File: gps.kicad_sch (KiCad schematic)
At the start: 9 parts, among them J6 SMA, U1 MAX-M10S

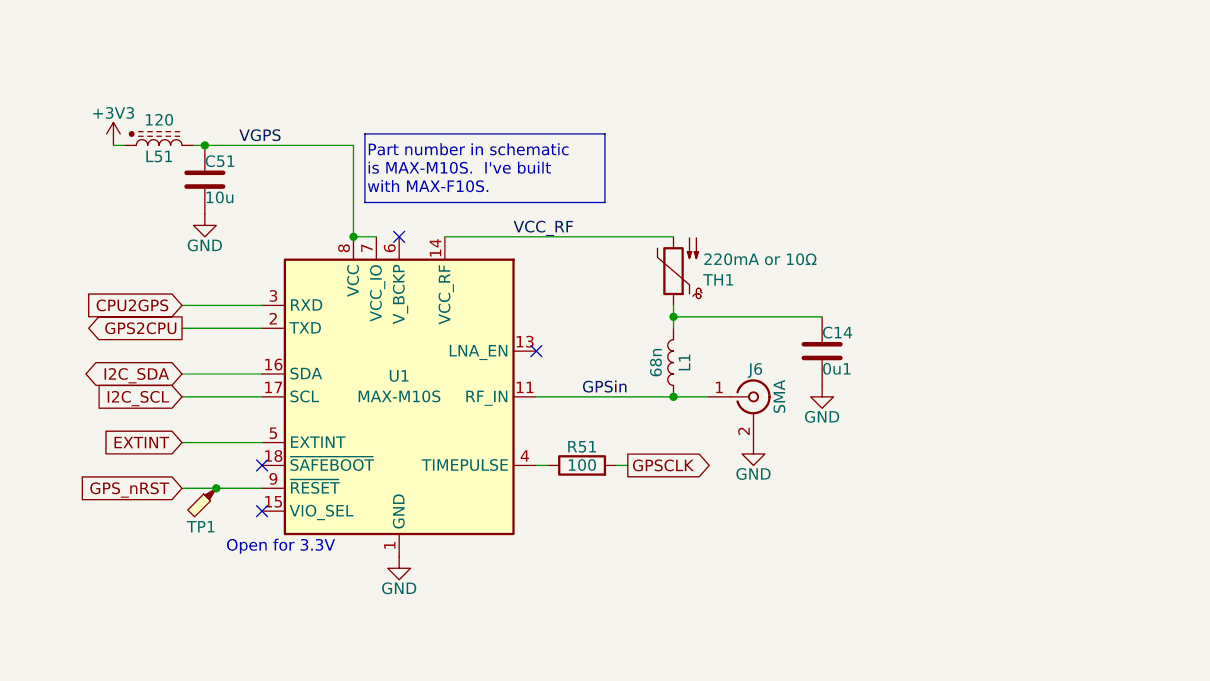
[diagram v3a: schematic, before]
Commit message: Pull-up on safe-boot.  Juggle things a bit.
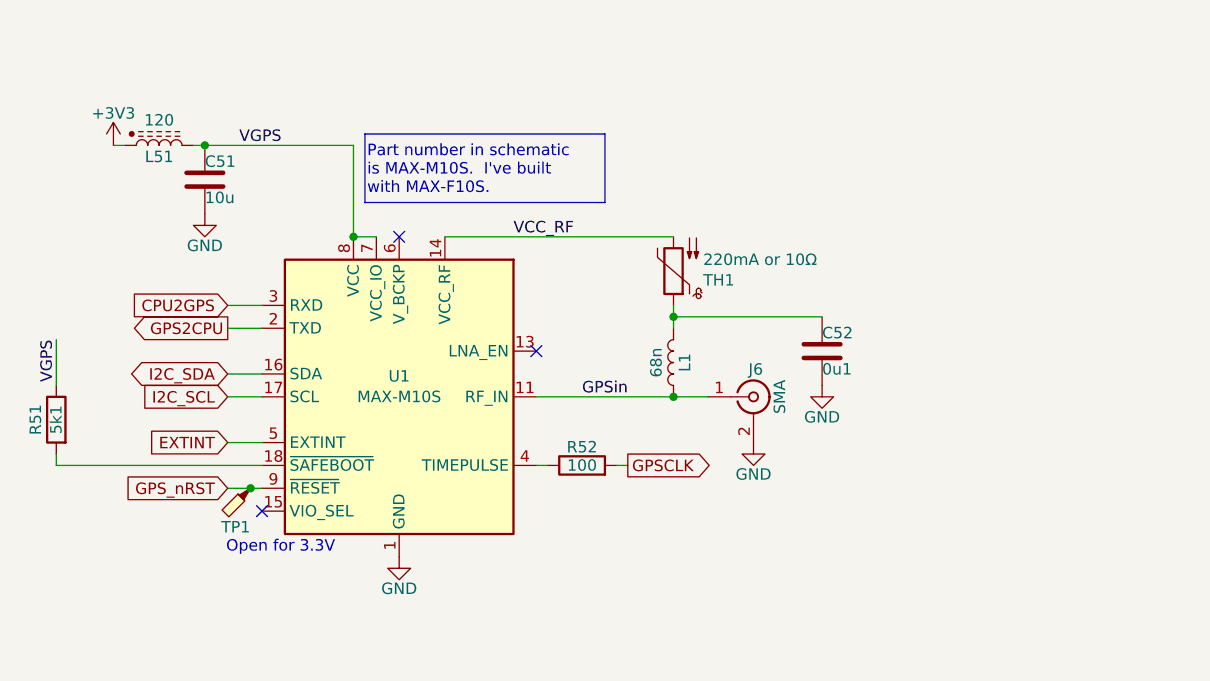
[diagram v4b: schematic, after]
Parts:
- added R51: 5k1, Resistor_SMD:R_0402_1005Metric, symbol Device:R
- renumbered C14 to C52, R51 to R52
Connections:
- net VGPS: now also R51.1
- net at U1.18 (~{SAFEBOOT}): now also R51.2
- no-connect marks 4 -> 3
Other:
- moved on the sheet: TP1
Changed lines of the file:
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@@
-	)
-	(junction
-		(at 80.01 109.22)
-		(diameter 0)
-		(color 0 0 0 0)
 	)
 	(junction
@@
 	)
 	(junction
+		(at 83.82 109.22)
+		(diameter 0)
+		(color 0 0 0 0)
+	)
+	(junction
 		(at 95.25 81.28)
 		(diameter 0)
@@
 	)
 	(no_connect
-		(at 85.09 106.68)
-	)
-	(no_connect
 		(at 100.33 81.28)
 	)
@@
 	(wire
 		(pts
-			(xy 80.01 109.22) (xy 85.09 109.22)
-		)
-		(stroke
-			(width 0)
-			(type default)
-		)
-	)
-	(wire
-		(pts
-			(xy 76.2 96.52) (xy 85.09 96.52)
+			(xy 81.28 96.52) (xy 85.09 96.52)
 		)
 		(stroke
@@
 	(wire
 		(pts
-			(xy 76.2 91.44) (xy 85.09 91.44)
+			(xy 81.28 91.44) (xy 85.09 91.44)
 		)
 		(stroke
@@
 	(wire
 		(pts
-			(xy 76.2 109.22) (xy 80.01 109.22)
+			(xy 81.28 109.22) (xy 83.82 109.22)
 		)
 		(stroke
@@
 	(wire
 		(pts
-			(xy 76.2 104.14) (xy 85.09 104.14)
+			(xy 62.23 106.68) (xy 85.09 106.68)
+		)
+		(stroke
+			(width 0)
+			(type default)
+		)
+	)
+	(wire
+		(pts
+			(xy 62.23 92.71) (xy 62.23 97.79)
+		)
+		(stroke
+			(width 0)
+			(type default)
+		)
+	)
+	(wire
+		(pts
+			(xy 81.28 104.14) (xy 85.09 104.14)
 		)
 		(stroke
@@
 	(wire
 		(pts
+			(xy 62.23 105.41) (xy 62.23 106.68)
+		)
+		(stroke
+			(width 0)
+			(type default)
+		)
+	)
+	(wire
+		(pts
 			(xy 130.81 88.9) (xy 130.81 90.17)
 		)
@@
 	(wire
 		(pts
-			(xy 76.2 88.9) (xy 85.09 88.9)
+			(xy 81.28 88.9) (xy 85.09 88.9)
 		)
 		(stroke
@@
 	(wire
 		(pts
-			(xy 76.2 99.06) (xy 85.09 99.06)
+			(xy 83.82 109.22) (xy 85.09 109.22)
+		)
+		(stroke
+			(width 0)
+			(type default)
+		)
+	)
+	(wire
+		(pts
+			(xy 81.28 99.06) (xy 85.09 99.06)
 		)
 		(stroke
@@
 	)
 	(label "VGPS"
+		(at 62.23 92.71 270)
+		(effects
+			(font
+				(size 1.27 1.27)
+			)
+			(justify right bottom)
+		)
+	)
+	(label "VGPS"
 		(at 82.55 71.12 0)
 		(effects
@@
 	(global_label "I2C_SCL"
 		(shape input)
-		(at 76.2 99.06 180)
-		(fields_autoplaced yes)
+		(at 81.28 99.06 180)
 		(effects
 			(font
@@
 		)
 		(property "Intersheetrefs" "${INTERSHEET_REFS}"
-			(at 65.6553 99.06 0)
+			(at 72.2593 99.06 0)
 			(show_name no)
 			(do_not_autoplace no)
@@
 	(global_label "I2C_SDA"
 		(shape bidirectional)
-		(at 76.2 96.52 180)
-		(fields_autoplaced yes)
+		(at 81.28 96.52 180)
 		(effects
 			(font
@@
 		)
 		(property "Intersheetrefs" "${INTERSHEET_REFS}"
-			(at 64.4835 96.52 0)
+			(at 71.0875 96.52 0)
 			(show_name no)
 			(do_not_autoplace no)
@@
 	(global_label "GPS2CPU"
 		(shape output)
-		(at 76.2 91.44 180)
-		(fields_autoplaced yes)
+		(at 81.28 91.44 180)
 		(effects
 			(font
@@
 		)
 		(property "Intersheetrefs" "${INTERSHEET_REFS}"
-			(at 64.3853 91.44 0)
+			(at 69.9733 91.44 0)
 			(show_name no)
 			(do_not_autoplace no)
@@
 	(global_label "GPS_nRST"
 		(shape input)
-		(at 76.2 109.22 180)
+		(at 81.28 109.22 180)
 		(fields_autoplaced yes)
 		(effects
@@
 		)
 		(property "Intersheetrefs" "${INTERSHEET_REFS}"
-			(at 63.9016 109.22 0)
+			(at 68.9816 109.22 0)
 			(show_name no)
 			(do_not_autoplace no)
@@
 	(global_label "CPU2GPS"
 		(shape input)
-		(at 76.2 88.9 180)
-		(fields_autoplaced yes)
+		(at 81.28 88.9 180)
 		(effects
 			(font
@@
 		)
 		(property "Intersheetrefs" "${INTERSHEET_REFS}"
-			(at 64.3853 88.9 0)
+			(at 70.7353 88.9 0)
 			(show_name no)
 			(do_not_autoplace no)
@@
 	(global_label "EXTINT"
 		(shape input)
-		(at 76.2 104.14 180)
+		(at 81.28 104.14 180)
 		(effects
 			(font
@@
 		)
 		(property "Intersheetrefs" "${INTERSHEET_REFS}"
-			(at 67.6509 104.14 0)
+			(at 73.4929 104.14 0)
 			(show_name no)
 			(do_not_autoplace no)
@@
 	(symbol
 		(lib_id "Connector:TestPoint_Probe")
-		(at 80.01 109.22 180)
+		(at 83.82 109.22 180)
 		(unit 1)
 		(body_style 1)
@@
 		(dnp no)
 		(property "Reference" "TP1"
-			(at 78.359 113.538 0)
+			(at 82.169 113.538 0)
 			(show_name no)
 			(do_not_autoplace no)
@@
 		)
 		(property "Value" "TestPoint_Probe"
-			(at 78.359 113.284 0)
+			(at 82.169 113.284 0)
 			(hide yes)
 			(show_name no)
@@
 		)
 		(property "Footprint" "Parts:TestPoint"
-			(at 74.93 109.22 0)
+			(at 78.74 109.22 0)
 			(hide yes)
 			(show_name no)
@@
 		)
 		(property "Datasheet" ""
-			(at 74.93 109.22 0)
+			(at 78.74 109.22 0)
 			(hide yes)
 			(show_name no)
@@
 		)
 		(property "Description" "test point (alternative probe-style design)"
-			(at 80.01 109.22 0)
+			(at 83.82 109.22 0)
 			(hide yes)
 			(show_name no)
@@
 		)
 		(property "Stock" "N/A"
-			(at 80.01 109.22 0)
+			(at 83.82 109.22 0)
 			(hide yes)
 			(show_name no)
@@
 	)
 	(symbol
+		(lib_id "Device:R")
+		(at 62.23 101.6 0)
+		(mirror y)
+		(unit 1)
+		(body_style 1)
+		(exclude_from_sim no)
+		(in_bom yes)
+		(on_board yes)
+		(in_pos_files yes)
+		(dnp no)
+		(property "Reference" "R51"
+			(at 59.944 101.6 90)
+			(show_name no)
+			(do_not_autoplace no)
+			(effects
+				(font
+					(size 1.27 1.27)
+				)
+			)
+		)
+		(property "Value" "5k1"
+			(at 62.23 101.6 90)
+			(show_name no)
+			(do_not_autoplace no)
+			(effects
+				(font
+					(size 1.27 1.27)
+				)
+			)
+		)
+		(property "Footprint" "Resistor_SMD:R_0402_1005Metric"
+			(at 64.008 101.6 90)
+			(hide yes)
+			(show_name no)
+			(do_not_autoplace no)
+			(effects
+				(font
+					(size 1.27 1.27)
+				)
+			)
+		)
+		(property "Datasheet" ""
+			(at 62.23 101.6 0)
+			(hide yes)
+			(show_name no)
+			(do_not_autoplace no)
+			(effects
+				(font
+					(size 1.27 1.27)
+				)
+			)
+		)
+		(property "Description" "Resistor"
+			(at 62.23 101.6 0)
+			(hide yes)
+			(show_name no)
+			(do_not_autoplace no)
+			(effects
+				(font
+					(size 1.27 1.27)
+				)
+			)
+		)
+		(property "LCSC" "C25905"
+			(at 62.23 101.6 90)
+			(hide yes)
+			(show_name no)
+			(do_not_autoplace no)
+			(effects
+				(font
+					(size 1.27 1.27)
+				)
+			)
+		)
+		(property "Stock" "Basic"
+			(at 62.23 101.6 90)
+			(hide yes)
+			(show_name no)
+			(do_not_autoplace no)
+			(effects
+				(font
+					(size 1.27 1.27)
+				)
+			)
+		)
+		(pin "2"
+		)
+		(pin "1"
+		)
+		(instances
+			(project "gpsfreak"
+				(path "/3160ff17-81c2-4674-af97-e8d9acaf6b65/69331f4b-e5ad-4452-8850-5c5a77857efb"
+					(reference "R51")
+					(unit 1)
+				)
+			)
+		)
+	)
+	(symbol
 		(lib_id "Device:C")
 		(at 147.32 93.98 0)
@@
 		(in_pos_files yes)
 		(dnp no)
-		(property "Reference" "C14"
+		(property "Reference" "C52"
 			(at 147.32 92.71 0)
 			(show_name no)
@@
 			(project "gpsfreak"
 				(path "/3160ff17-81c2-4674-af97-e8d9acaf6b65/69331f4b-e5ad-4452-8850-5c5a77857efb"
-					(reference "C14")
+					(reference "C52")
 					(unit 1)
 				)
@@
 		(in_pos_files yes)
 		(dnp no)
-		(property "Reference" "R51"
+		(property "Reference" "R52"
 			(at 120.65 104.648 90)
 			(show_name no)
@@
 			(project "gpsfreak"
 				(path "/3160ff17-81c2-4674-af97-e8d9acaf6b65/69331f4b-e5ad-4452-8850-5c5a77857efb"
-					(reference "R51")
+					(reference "R52")
 					(unit 1)
 				)

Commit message: Ordered.
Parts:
- TH1: Stock Ok -> 3
- U1: Stock ORDER, 1 -> ORDER
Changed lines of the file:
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@@
 			)
 		)
-		(property "Stock" "Ok"
+		(property "Stock" "3"
 			(at 130.81 85.09 0)
 			(hide yes)
@@
 			)
 		)
-		(property "Stock" "ORDER, 1"
-			(at 100.33 99.06 0)
-			(hide yes)
+		(property "Stock" "ORDER"
+			(at 100.33 99.06 0)
+			(hide yes)

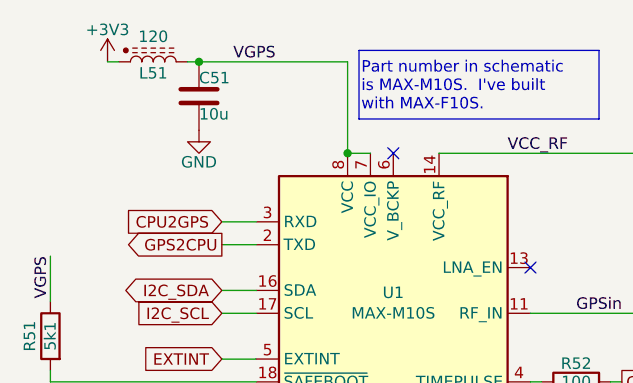
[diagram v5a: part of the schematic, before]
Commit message: Adjustments.  Silk screen clearance.
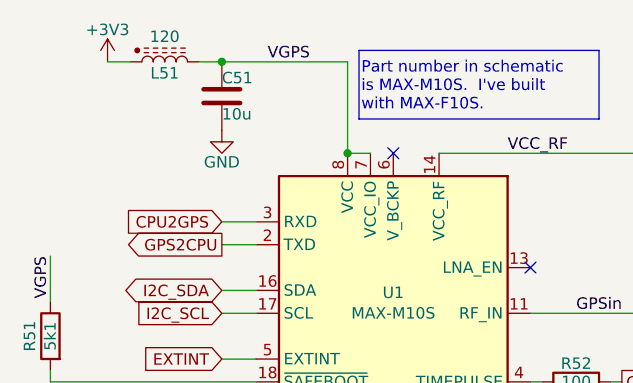
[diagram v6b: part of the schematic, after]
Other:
- moved on the sheet: C51, L51
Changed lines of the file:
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@@
-	)
-	(junction
-		(at 78.74 71.12)
-		(diameter 0)
-		(color 0 0 0 0)
 	)
 	(junction
@@
 	)
 	(junction
+		(at 81.28 71.12)
+		(diameter 0)
+		(color 0 0 0 0)
+	)
+	(junction
 		(at 83.82 109.22)
 		(diameter 0)
@@
 	(wire
 		(pts
+			(xy 81.28 71.12) (xy 95.25 71.12)
+		)
+		(stroke
+			(width 0)
+			(type default)
+		)
+	)
+	(wire
+		(pts
 			(xy 81.28 91.44) (xy 85.09 91.44)
 		)
@@
 	(wire
 		(pts
-			(xy 68.58 71.12) (xy 69.85 71.12)
+			(xy 68.58 71.12) (xy 71.12 71.12)
 		)
 		(stroke
@@
 	(wire
 		(pts
-			(xy 77.47 71.12) (xy 78.74 71.12)
-		)
-		(stroke
-			(width 0)
-			(type default)
-		)
-	)
-	(wire
-		(pts
-			(xy 78.74 71.12) (xy 95.25 71.12)
+			(xy 78.74 71.12) (xy 81.28 71.12)
 		)
 		(stroke
@@
 	)
 	(label "VGPS"
-		(at 82.55 71.12 0)
+		(at 86.36 71.12 0)
 		(effects
 			(font
@@
 		(shape input)
 		(at 81.28 109.22 180)
-		(fields_autoplaced yes)
 		(effects
 			(font
@@
 		)
 		(property "Intersheetrefs" "${INTERSHEET_REFS}"
-			(at 68.9816 109.22 0)
+			(at 70.2516 109.22 0)
 			(show_name no)
 			(do_not_autoplace no)
@@
 	(symbol
 		(lib_id "Parts:L_Ferrite_Power")
-		(at 73.66 71.12 90)
+		(at 74.93 71.12 90)
 		(unit 1)
 		(body_style 1)
@@
 		(dnp no)
 		(property "Reference" "L51"
-			(at 73.66 72.39 90)
+			(at 74.93 72.39 90)
 			(show_name no)
 			(do_not_autoplace no)
@@
 		)
 		(property "Value" "120"
-			(at 73.66 68.326 90)
+			(at 74.93 68.326 90)
 			(show_name no)
 			(do_not_autoplace no)
@@
 		)
 		(property "Footprint" "Inductor_SMD:L_0603_1608Metric"
-			(at 73.66 71.12 0)
+			(at 74.93 71.12 0)
 			(hide yes)
 			(show_name no)
@@
 		)
 		(property "Datasheet" ""
-			(at 73.66 71.12 0)
+			(at 74.93 71.12 0)
 			(hide yes)
 			(show_name no)
@@
 		)
 		(property "Description" "Inductor with ferrite core"
-			(at 73.66 71.12 0)
+			(at 74.93 71.12 0)
 			(hide yes)
 			(show_name no)
@@
 		)
 		(property "LCSC" "C14709"
-			(at 73.66 71.12 90)
+			(at 74.93 71.12 90)
 			(hide yes)
 			(show_name no)
@@
 		)
 		(property "Stock" "Basic"
-			(at 73.66 71.12 90)
+			(at 74.93 71.12 90)
 			(hide yes)
 			(show_name no)
@@
 	(symbol
 		(lib_id "Device:C")
-		(at 78.74 74.93 0)
+		(at 81.28 74.93 0)
 		(unit 1)
 		(body_style 1)
@@
 		(dnp no)
 		(property "Reference" "C51"
-			(at 78.74 73.66 0)
+			(at 81.28 73.66 0)
 			(show_name no)
 			(do_not_autoplace no)
@@
 		)
 		(property "Value" "10u"
-			(at 78.74 76.2 0)
+			(at 81.28 76.2 0)
 			(show_name no)
 			(do_not_autoplace no)
@@
 		)
 		(property "Footprint" "Capacitor_SMD:C_0402_1005Metric"
-			(at 79.7052 78.74 0)
+			(at 82.2452 78.74 0)
 			(hide yes)
 			(show_name no)
@@
 		)
 		(property "Datasheet" ""
-			(at 78.74 74.93 0)
+			(at 81.28 74.93 0)
 			(hide yes)
 			(show_name no)
@@
 		)
 		(property "Description" "Unpolarized capacitor"
-			(at 78.74 74.93 0)
+			(at 81.28 74.93 0)
 			(hide yes)
 			(show_name no)
@@
 		)
 		(property "LCSC" "C15525"
-			(at 78.74 74.93 0)
+			(at 81.28 74.93 0)
 			(hide yes)
 			(show_name no)
@@
 		)
 		(property "Stock" "Basic"
-			(at 78.74 74.93 0)
+			(at 81.28 74.93 0)
 			(hide yes)
 			(show_name no)
@@
 	(symbol
 		(lib_id "power:GND")
-		(at 78.74 78.74 0)
+		(at 81.28 78.74 0)
 		(unit 1)
 		(body_style 1)
@@
 		(dnp no)
 		(property "Reference" "#PWR028"
-			(at 78.74 85.09 0)
+			(at 81.28 85.09 0)
 			(hide yes)
 			(show_name no)
@@
 		)
 		(property "Value" "GND"
-			(at 78.74 81.534 0)
+			(at 81.28 81.534 0)
 			(show_name no)
 			(do_not_autoplace no)
@@
 		)
 		(property "Footprint" ""
-			(at 78.74 78.74 0)
+			(at 81.28 78.74 0)
 			(hide yes)
 			(show_name no)
@@
 		)
 		(property "Datasheet" ""
-			(at 78.74 78.74 0)
+			(at 81.28 78.74 0)
 			(hide yes)
 			(show_name no)
@@
 		)
 		(property "Description" "Power symbol creates a global label with name \"GND\" , ground"
-			(at 78.74 78.74 0)
-			(hide yes)
-			(show_name no)
+			(at 81.28 78.74 0)
+			(hide yes)
+			(show_name no)

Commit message: Change the 10µF 0402 part number.
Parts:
- C51: LCSC C15525 -> C315248; Stock Basic -> Ext
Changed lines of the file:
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@@
 			)
 		)
-		(property "Datasheet" ""
+		(property "Datasheet" "10V"
 			(at 81.28 74.93 0)
 			(hide yes)
@@
 			)
 		)
-		(property "LCSC" "C15525"
+		(property "LCSC" "C315248"
 			(at 81.28 74.93 0)
 			(hide yes)
@@
 			)
 		)
-		(property "Stock" "Basic"
+		(property "Stock" "Ext"
 			(at 81.28 74.93 0)
 			(hide yes)
